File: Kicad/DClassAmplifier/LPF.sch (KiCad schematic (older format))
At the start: 12 parts

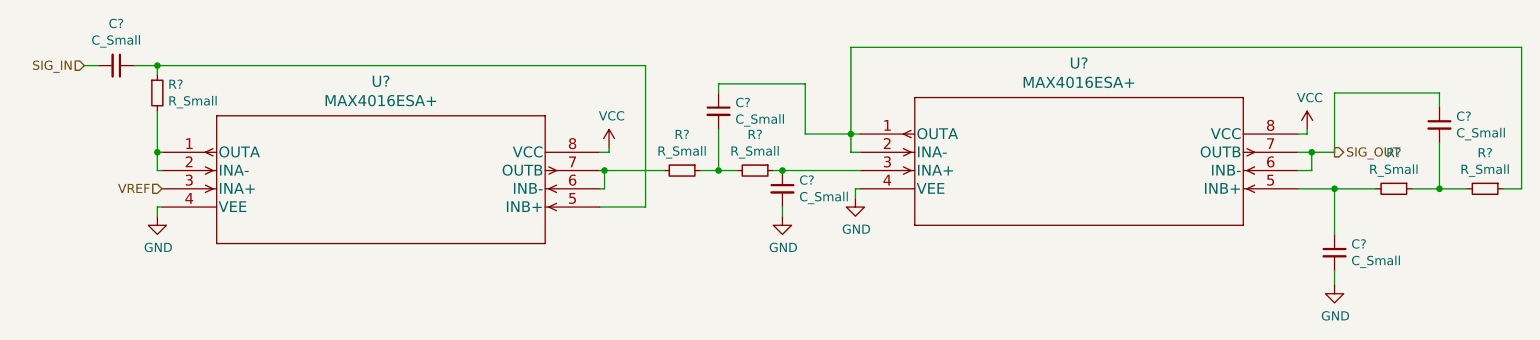
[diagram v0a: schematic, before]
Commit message: Finish off Main Part of Schematic
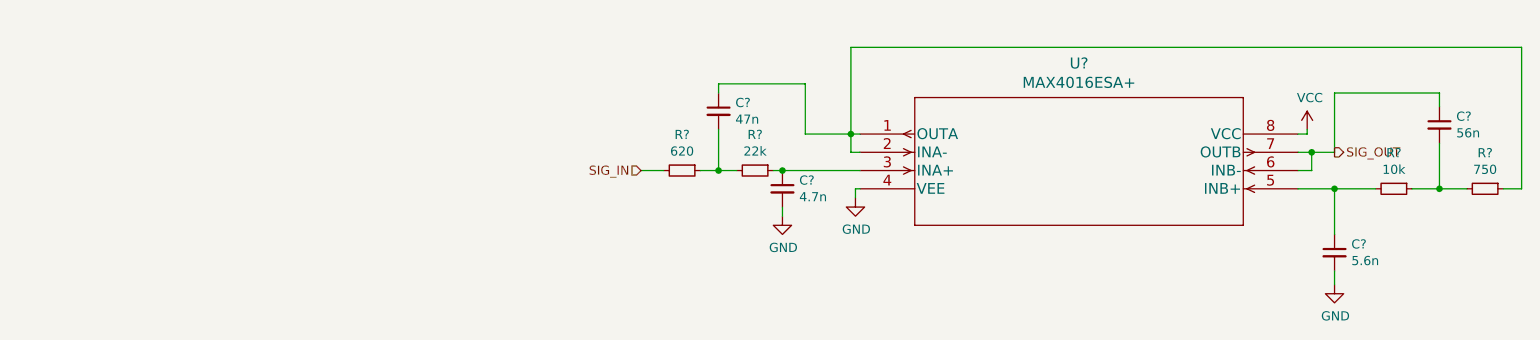
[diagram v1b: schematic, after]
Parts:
- removed C?: C_Small, symbol Device:C_Small
- removed R?: R_Small, symbol Device:R_Small
- removed U?: MAX4016ESA+, 21-0041B_8_MXM, symbol MAX4016ESA:MAX4016ESA+
- C?: value C_Small -> 4.7n; footprint (none) -> Capacitor_SMD:C_0603_1608Metric_Pad1.08x0.95mm_HandSolder
- C?: value C_Small -> 47n; footprint (none) -> Capacitor_SMD:C_0603_1608Metric_Pad1.08x0.95mm_HandSolder
- C?: value C_Small -> 5.6n; footprint (none) -> Capacitor_SMD:C_0603_1608Metric_Pad1.08x0.95mm_HandSolder
- C?: value C_Small -> 56n; footprint (none) -> Capacitor_SMD:C_0603_1608Metric_Pad1.08x0.95mm_HandSolder
- R?: value R_Small -> 22k; footprint (none) -> Resistor_SMD:R_0603_1608Metric_Pad0.98x0.95mm_HandSolder
- R?: value R_Small -> 620; footprint (none) -> Resistor_SMD:R_0603_1608Metric_Pad0.98x0.95mm_HandSolder
- R?: value R_Small -> 10k; footprint (none) -> Resistor_SMD:R_0603_1608Metric_Pad0.98x0.95mm_HandSolder
- R?: value R_Small -> 750; footprint (none) -> Resistor_SMD:R_0603_1608Metric_Pad0.98x0.95mm_HandSolder
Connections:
- net SIG_IN: now also R?.2
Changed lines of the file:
@@
 $Descr A4 11693 8268
 encoding utf-8
-Sheet 5 6
+Sheet 7 7
 Title ""
 Date ""
@@
 $Comp
 L MAX4016ESA:MAX4016ESA+ U?
-U 1 1 61194A75
-P 3650 3325
-F 0 "U?" H 4850 3712 60  0000 C CNN
-F 1 "MAX4016ESA+" H 4850 3606 60  0000 C CNN
-F 2 "21-0041B_8_MXM" H 4850 3565 60  0001 C CNN
-F 3 "" H 3650 3325 60  0000 C CNN
-	1    3650 3325
-	1    0    0    -1
-$EndComp
-$Comp
-L MAX4016ESA:MAX4016ESA+ U?
 U 1 1 61194DD9
 P 7475 3225
@@
 	1    0    0    -1
 $EndComp
-$Comp
-L power:VCC #PWR?
-U 1 1 61196119
-P 6100 3300
-F 0 "#PWR?" H 6100 3150 50  0001 C CNN
-F 1 "VCC" H 6115 3473 50  0000 C CNN
-F 2 "" H 6100 3300 50  0001 C CNN
-F 3 "" H 6100 3300 50  0001 C CNN
-	1    6100 3300
-	1    0    0    -1
-$EndComp
-Wire Wire Line
-	6100 3300 6100 3325
-Wire Wire Line
-	6100 3325 6050 3325
 $Comp
 L power:VCC #PWR?
@@
 	7450 3525 7475 3525
 $Comp
-L power:GND #PWR?
-U 1 1 61198F46
-P 3625 3675
-F 0 "#PWR?" H 3625 3425 50  0001 C CNN
-F 1 "GND" H 3630 3502 50  0000 C CNN
-F 2 "" H 3625 3675 50  0001 C CNN
-F 3 "" H 3625 3675 50  0001 C CNN
-	1    3625 3675
-	1    0    0    -1
-$EndComp
-Wire Wire Line
-	3650 3625 3625 3625
-Wire Wire Line
-	3625 3625 3625 3675
-Text HLabel 3650 3525 0    50   Input ~ 0
-VREF
-Wire Wire Line
-	3650 3425 3625 3425
-Wire Wire Line
-	3625 3425 3625 3325
-Wire Wire Line
-	3625 3325 3650 3325
-$Comp
-L Device:R_Small R?
-U 1 1 6119A6EB
-P 3625 3000
-F 0 "R?" H 3684 3046 50  0000 L CNN
-F 1 "R_Small" H 3684 2955 50  0000 L CNN
-F 2 "" H 3625 3000 50  0001 C CNN
-F 3 "~" H 3625 3000 50  0001 C CNN
-	1    3625 3000
-	1    0    0    -1
-$EndComp
-Wire Wire Line
-	3625 3100 3625 3325
-Connection ~ 3625 3325
-$Comp
-L Device:C_Small C?
-U 1 1 6119BD91
-P 3400 2850
-F 0 "C?" V 3171 2850 50  0000 C CNN
-F 1 "C_Small" V 3262 2850 50  0000 C CNN
-F 2 "" H 3400 2850 50  0001 C CNN
-F 3 "~" H 3400 2850 50  0001 C CNN
-	1    3400 2850
-	0    1    1    0
-$EndComp
-Wire Wire Line
-	3500 2850 3625 2850
-Wire Wire Line
-	3625 2850 3625 2900
-Text HLabel 3225 2850 0    50   Input ~ 0
-SIG_IN
-Wire Wire Line
-	3225 2850 3300 2850
-Wire Wire Line
-	6050 3425 6075 3425
-Wire Wire Line
-	6075 3425 6075 3525
-Wire Wire Line
-	6075 3525 6050 3525
-Wire Wire Line
-	3625 2850 6300 2850
-Wire Wire Line
-	6300 2850 6300 3625
-Wire Wire Line
-	6300 3625 6050 3625
-Connection ~ 3625 2850
-$Comp
 L Device:R_Small R?
 U 1 1 6119FD9F
 P 6900 3425
 F 0 "R?" V 6704 3425 50  0000 C CNN
-F 1 "R_Small" V 6795 3425 50  0000 C CNN
-F 2 "" H 6900 3425 50  0001 C CNN
+F 1 "22k" V 6795 3425 50  0000 C CNN
+F 2 "Resistor_SMD:R_0603_1608Metric_Pad0.98x0.95mm_HandSolder" H 6900 3425 50  0001 C CNN
 F 3 "~" H 6900 3425 50  0001 C CNN
 	1    6900 3425
@@
 P 6500 3425
 F 0 "R?" V 6304 3425 50  0000 C CNN
-F 1 "R_Small" V 6395 3425 50  0000 C CNN
-F 2 "" H 6500 3425 50  0001 C CNN
+F 1 "620" V 6395 3425 50  0000 C CNN
+F 2 "Resistor_SMD:R_0603_1608Metric_Pad0.98x0.95mm_HandSolder" H 6500 3425 50  0001 C CNN
 F 3 "~" H 6500 3425 50  0001 C CNN
 	1    6500 3425
@@
 P 7050 3525
 F 0 "C?" H 7142 3571 50  0000 L CNN
-F 1 "C_Small" H 7142 3480 50  0000 L CNN
-F 2 "" H 7050 3525 50  0001 C CNN
+F 1 "4.7n" H 7142 3480 50  0000 L CNN
+F 2 "Capacitor_SMD:C_0603_1608Metric_Pad1.08x0.95mm_HandSolder" H 7050 3525 50  0001 C CNN
 F 3 "~" H 7050 3525 50  0001 C CNN
 	1    7050 3525
@@
 P 6700 3100
 F 0 "C?" H 6792 3146 50  0000 L CNN
-F 1 "C_Small" H 6792 3055 50  0000 L CNN
-F 2 "" H 6700 3100 50  0001 C CNN
+F 1 "47n" H 6792 3055 50  0000 L CNN
+F 2 "Capacitor_SMD:C_0603_1608Metric_Pad1.08x0.95mm_HandSolder" H 6700 3100 50  0001 C CNN
 F 3 "~" H 6700 3100 50  0001 C CNN
 	1    6700 3100
@@
 Wire Wire Line
 	7425 3225 7175 3225
-Wire Wire Line
-	6400 3425 6075 3425
-Connection ~ 6075 3425
 $Comp
 L Device:C_Small C?
@@
 P 10075 3875
 F 0 "C?" H 10167 3921 50  0000 L CNN
-F 1 "C_Small" H 10167 3830 50  0000 L CNN
-F 2 "" H 10075 3875 50  0001 C CNN
+F 1 "5.6n" H 10167 3830 50  0000 L CNN
+F 2 "Capacitor_SMD:C_0603_1608Metric_Pad1.08x0.95mm_HandSolder" H 10075 3875 50  0001 C CNN
 F 3 "~" H 10075 3875 50  0001 C CNN
 	1    10075 3875
@@
 P 10400 3525
 F 0 "R?" V 10204 3525 50  0000 C CNN
-F 1 "R_Small" V 10295 3525 50  0000 C CNN
-F 2 "" H 10400 3525 50  0001 C CNN
+F 1 "10k" V 10295 3525 50  0000 C CNN
+F 2 "Resistor_SMD:R_0603_1608Metric_Pad0.98x0.95mm_HandSolder" H 10400 3525 50  0001 C CNN
 F 3 "~" H 10400 3525 50  0001 C CNN
 	1    10400 3525
@@
 P 10900 3525
 F 0 "R?" V 10704 3525 50  0000 C CNN
-F 1 "R_Small" V 10795 3525 50  0000 C CNN
-F 2 "" H 10900 3525 50  0001 C CNN
+F 1 "750" V 10795 3525 50  0000 C CNN
+F 2 "Resistor_SMD:R_0603_1608Metric_Pad0.98x0.95mm_HandSolder" H 10900 3525 50  0001 C CNN
 F 3 "~" H 10900 3525 50  0001 C CNN
 	1    10900 3525
@@
 P 10650 3175
 F 0 "C?" H 10742 3221 50  0000 L CNN
-F 1 "C_Small" H 10742 3130 50  0000 L CNN
-F 2 "" H 10650 3175 50  0001 C CNN
+F 1 "56n" H 10742 3130 50  0000 L CNN
+F 2 "Capacitor_SMD:C_0603_1608Metric_Pad1.08x0.95mm_HandSolder" H 10650 3175 50  0001 C CNN
 F 3 "~" H 10650 3175 50  0001 C CNN
 	1    10650 3175
@@
 Text HLabel 10075 3325 2    50   Output ~ 0
 SIG_OUT
+Text HLabel 6275 3425 0    50   Input ~ 0
+SIG_IN
+Wire Wire Line
+	6275 3425 6400 3425
 $EndSCHEMATC

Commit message: updates to schematic
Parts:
- gave numbers to parts that had none: 9
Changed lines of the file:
@@
 $EndDescr
 $Comp
-L MAX4016ESA:MAX4016ESA+ U?
+L MAX4016ESA:MAX4016ESA+ U4
 U 1 1 61194DD9
 P 7475 3225
-F 0 "U?" H 8675 3612 60  0000 C CNN
+F 0 "U4" H 8675 3612 60  0000 C CNN
 F 1 "MAX4016ESA+" H 8675 3506 60  0000 C CNN
 F 2 "21-0041B_8_MXM" H 8675 3465 60  0001 C CNN
@@
 $EndComp
 $Comp
-L power:VCC #PWR?
+L power:VCC #PWR0141
 U 1 1 61197634
 P 9925 3200
-F 0 "#PWR?" H 9925 3050 50  0001 C CNN
+F 0 "#PWR0141" H 9925 3050 50  0001 C CNN
 F 1 "VCC" H 9940 3373 50  0000 C CNN
 F 2 "" H 9925 3200 50  0001 C CNN
@@
 	9925 3225 9875 3225
 $Comp
-L power:GND #PWR?
+L power:GND #PWR0142
 U 1 1 61197F03
 P 7450 3575
-F 0 "#PWR?" H 7450 3325 50  0001 C CNN
+F 0 "#PWR0142" H 7450 3325 50  0001 C CNN
 F 1 "GND" H 7455 3402 50  0000 C CNN
 F 2 "" H 7450 3575 50  0001 C CNN
@@
 	7450 3525 7475 3525
 $Comp
-L Device:R_Small R?
+L Device:R_Small R17
 U 1 1 6119FD9F
 P 6900 3425
-F 0 "R?" V 6704 3425 50  0000 C CNN
+F 0 "R17" V 6704 3425 50  0000 C CNN
 F 1 "22k" V 6795 3425 50  0000 C CNN
 F 2 "Resistor_SMD:R_0603_1608Metric_Pad0.98x0.95mm_HandSolder" H 6900 3425 50  0001 C CNN
@@
 $EndComp
 $Comp
-L Device:R_Small R?
+L Device:R_Small R16
 U 1 1 611A0CB6
 P 6500 3425
-F 0 "R?" V 6304 3425 50  0000 C CNN
+F 0 "R16" V 6304 3425 50  0000 C CNN
 F 1 "620" V 6395 3425 50  0000 C CNN
 F 2 "Resistor_SMD:R_0603_1608Metric_Pad0.98x0.95mm_HandSolder" H 6500 3425 50  0001 C CNN
@@
 $EndComp
 $Comp
-L Device:C_Small C?
+L Device:C_Small C12
 U 1 1 611A751B
 P 7050 3525
-F 0 "C?" H 7142 3571 50  0000 L CNN
+F 0 "C12" H 7142 3571 50  0000 L CNN
 F 1 "4.7n" H 7142 3480 50  0000 L CNN
 F 2 "Capacitor_SMD:C_0603_1608Metric_Pad1.08x0.95mm_HandSolder" H 7050 3525 50  0001 C CNN
@@
 $EndComp
 $Comp
-L Device:C_Small C?
+L Device:C_Small C11
 U 1 1 611A7CBC
 P 6700 3100
-F 0 "C?" H 6792 3146 50  0000 L CNN
+F 0 "C11" H 6792 3146 50  0000 L CNN
 F 1 "47n" H 6792 3055 50  0000 L CNN
 F 2 "Capacitor_SMD:C_0603_1608Metric_Pad1.08x0.95mm_HandSolder" H 6700 3100 50  0001 C CNN
@@
 	7050 3625 7050 3675
 $Comp
-L power:GND #PWR?
+L power:GND #PWR0143
 U 1 1 611AAC29
 P 7050 3675
-F 0 "#PWR?" H 7050 3425 50  0001 C CNN
+F 0 "#PWR0143" H 7050 3425 50  0001 C CNN
 F 1 "GND" H 7055 3502 50  0000 C CNN
 F 2 "" H 7050 3675 50  0001 C CNN
@@
 	7425 3225 7175 3225
 $Comp
-L Device:C_Small C?
+L Device:C_Small C13
 U 1 1 611BBE57
 P 10075 3875
-F 0 "C?" H 10167 3921 50  0000 L CNN
+F 0 "C13" H 10167 3921 50  0000 L CNN
 F 1 "5.6n" H 10167 3830 50  0000 L CNN
 F 2 "Capacitor_SMD:C_0603_1608Metric_Pad1.08x0.95mm_HandSolder" H 10075 3875 50  0001 C CNN
@@
 $EndComp
 $Comp
-L Device:R_Small R?
+L Device:R_Small R18
 U 1 1 611BC850
 P 10400 3525
-F 0 "R?" V 10204 3525 50  0000 C CNN
+F 0 "R18" V 10204 3525 50  0000 C CNN
 F 1 "10k" V 10295 3525 50  0000 C CNN
 F 2 "Resistor_SMD:R_0603_1608Metric_Pad0.98x0.95mm_HandSolder" H 10400 3525 50  0001 C CNN
@@
 $EndComp
 $Comp
-L Device:R_Small R?
+L Device:R_Small R19
 U 1 1 611BD0E0
 P 10900 3525
-F 0 "R?" V 10704 3525 50  0000 C CNN
+F 0 "R19" V 10704 3525 50  0000 C CNN
 F 1 "750" V 10795 3525 50  0000 C CNN
 F 2 "Resistor_SMD:R_0603_1608Metric_Pad0.98x0.95mm_HandSolder" H 10900 3525 50  0001 C CNN
@@
 	11100 3525 11000 3525
 $Comp
-L Device:C_Small C?
+L Device:C_Small C14
 U 1 1 611C0153
 P 10650 3175
-F 0 "C?" H 10742 3221 50  0000 L CNN
+F 0 "C14" H 10742 3221 50  0000 L CNN
 F 1 "56n" H 10742 3130 50  0000 L CNN
 F 2 "Capacitor_SMD:C_0603_1608Metric_Pad1.08x0.95mm_HandSolder" H 10650 3175 50  0001 C CNN
@@
 	10650 3525 10800 3525
 $Comp
-L power:GND #PWR?
+L power:GND #PWR0144
 U 1 1 611C31DE
 P 10075 4050
-F 0 "#PWR?" H 10075 3800 50  0001 C CNN
+F 0 "#PWR0144" H 10075 3800 50  0001 C CNN
 F 1 "GND" H 10080 3877 50  0000 C CNN
 F 2 "" H 10075 4050 50  0001 C CNN

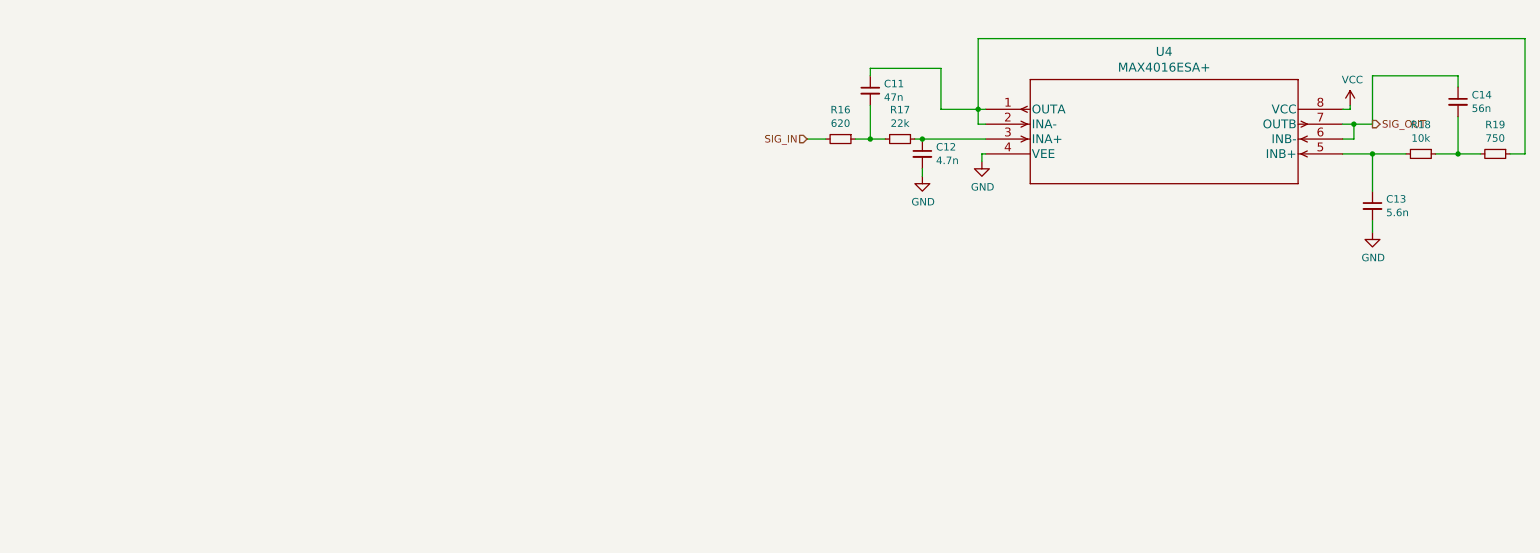
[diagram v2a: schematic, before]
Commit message: Update Opamp for Input Filter
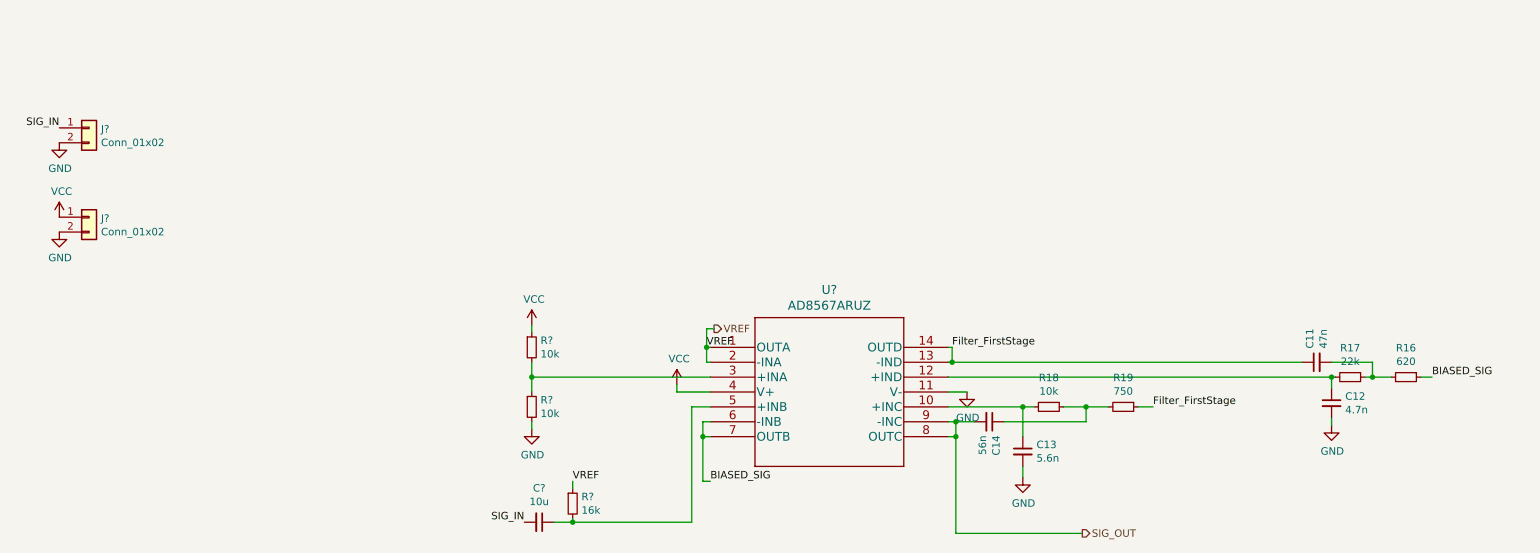
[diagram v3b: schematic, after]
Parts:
- removed U4: MAX4016ESA+, 21-0041B_8_MXM, symbol MAX4016ESA:MAX4016ESA+
- added C?: 10u, Capacitor_SMD:C_0805_2012Metric_Pad1.18x1.45mm_HandSolder, symbol Device:C_Small
- added J? (x2): Conn_01x02, symbol Connector_Generic:Conn_01x02
- added R?: 16k, Resistor_SMD:R_0603_1608Metric_Pad0.98x0.95mm_HandSolder, symbol Device:R_Small
- added R? (x2): 10k, Resistor_SMD:R_0603_1608Metric_Pad0.98x0.95mm_HandSolder, symbol Device:R_Small
- added U?: AD8567ARUZ, RU_14_ADI, symbol AD8567ARUZ:AD8567ARUZ
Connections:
- net GND: now also J?.2 (Pin_2), J?.2 (Pin_2), R?.2, U?.11 (V-)
- net SIG_IN: now also C?.2, J?.1 (Pin_1); no longer R16.2
- net SIG_OUT: now also C14.2, U?.8 (OUTC), U?.9 (-INC); no longer C14.1
- net VCC: now also J?.1 (Pin_1), R?.1, U?.4 (V+)
- net Filter_FirstStage: now reaches C11.1, R19.1
- net Filter_FirstStage: now also U?.13 (-IND), U?.14 (OUTD)
- net at C12.1: now also R17.2, U?.12 (+IND); no longer R17.1
- net at C13.1, R18.2: now also U?.10 (+INC)
- net at R18.1, R19.2: now also C14.1; no longer C14.2
- new net: R?.1, R?.2, U?.3 (+INA)
- new net: C?.1, R?.2, U?.5 (+INB)
- new net: C11.2, R16.2, R17.1
- new net BIASED_SIG: R16.1, U?.6 (-INB), U?.7 (OUTB)
- new net VREF: R?.1, U?.1 (OUTA), U?.2 (-INA)
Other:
- moved on the sheet: C11, C12, C13, C14, R16, R17, R18, R19

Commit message: Added footprints to schematic
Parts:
- J5, J6: renamed from J?; footprint (none) -> Connector_PinSocket_2.54mm:PinSocket_1x02_P2.54mm_Vertical
- gave numbers to parts that had none: 5
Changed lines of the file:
@@
 SIG_OUT
 $Comp
-L AD8567ARUZ:AD8567ARUZ U?
+L AD8567ARUZ:AD8567ARUZ U3
 U 1 1 61100E74
 P 5625 4825
-F 0 "U?" H 6425 5212 60  0000 C CNN
+F 0 "U3" H 6425 5212 60  0000 C CNN
 F 1 "AD8567ARUZ" H 6425 5106 60  0000 C CNN
 F 2 "RU_14_ADI" H 6425 5065 60  0001 C CNN
@@
 $EndComp
 $Comp
-L power:VCC #PWR?
+L power:VCC #PWR0134
 U 1 1 61106B01
 P 5400 5075
-AR Path="/610C616D/61106B01" Ref="#PWR?"  Part="1"
+AR Path="/610C616D/61106B01" Ref="#PWR0134"  Part="1"
 AR Path="/611D4178/61106B01" Ref="#PWR?"  Part="1"
-F 0 "#PWR?" H 5400 4925 50  0001 C CNN
+F 0 "#PWR0134" H 5400 4925 50  0001 C CNN
 F 1 "VCC" H 5415 5248 50  0000 C CNN
 F 2 "" H 5400 5075 50  0001 C CNN
@@
 $EndComp
 $Comp
-L power:GND #PWR?
+L power:GND #PWR0135
 U 1 1 61106B09
 P 7350 5125
-AR Path="/610C616D/61106B09" Ref="#PWR?"  Part="1"
+AR Path="/610C616D/61106B09" Ref="#PWR0135"  Part="1"
 AR Path="/611D4178/61106B09" Ref="#PWR?"  Part="1"
-F 0 "#PWR?" H 7350 4875 50  0001 C CNN
+F 0 "#PWR0135" H 7350 4875 50  0001 C CNN
 F 1 "GND" H 7355 4952 50  0000 C CNN
 F 2 "" H 7350 5125 50  0001 C CNN
@@
 	5600 4825 5625 4825
 $Comp
-L Device:R_Small R?
+L Device:R_Small R15
 U 1 1 61106B14
 P 4700 5875
-AR Path="/610C616D/61106B14" Ref="R?"  Part="1"
+AR Path="/610C616D/61106B14" Ref="R15"  Part="1"
 AR Path="/611D4178/61106B14" Ref="R?"  Part="1"
-F 0 "R?" H 4759 5921 50  0000 L CNN
+F 0 "R15" H 4759 5921 50  0000 L CNN
 F 1 "16k" H 4759 5830 50  0000 L CNN
 F 2 "Resistor_SMD:R_0603_1608Metric_Pad0.98x0.95mm_HandSolder" H 4700 5875 50  0001 C CNN
@@
 Connection ~ 5600 4825
 $Comp
-L Device:C_Small C?
+L Device:C_Small C10
 U 1 1 61106B1C
 P 4475 6000
-AR Path="/610C616D/61106B1C" Ref="C?"  Part="1"
+AR Path="/610C616D/61106B1C" Ref="C10"  Part="1"
 AR Path="/611D4178/61106B1C" Ref="C?"  Part="1"
-F 0 "C?" V 4246 6000 50  0000 C CNN
+F 0 "C10" V 4246 6000 50  0000 C CNN
 F 1 "10u" V 4337 6000 50  0000 C CNN
 F 2 "Capacitor_SMD:C_0805_2012Metric_Pad1.18x1.45mm_HandSolder" H 4475 6000 50  0001 C CNN
@@
 P 4425 4825
 AR Path="/611D4178/61106B32" Ref="R?"  Part="1"
-AR Path="/610C616D/61106B32" Ref="R?"  Part="1"
-F 0 "R?" H 4484 4871 50  0000 L CNN
+AR Path="/610C616D/61106B32" Ref="R13"  Part="1"
+F 0 "R13" H 4484 4871 50  0000 L CNN
 F 1 "10k" H 4484 4780 50  0000 L CNN
 F 2 "Resistor_SMD:R_0603_1608Metric_Pad0.98x0.95mm_HandSolder" H 4425 4825 50  0001 C CNN
@@
 P 4425 5375
 AR Path="/611D4178/61106B3C" Ref="#PWR?"  Part="1"
-AR Path="/610C616D/61106B3C" Ref="#PWR?"  Part="1"
-F 0 "#PWR?" H 4425 5125 50  0001 C CNN
+AR Path="/610C616D/61106B3C" Ref="#PWR0136"  Part="1"
+F 0 "#PWR0136" H 4425 5125 50  0001 C CNN
 F 1 "GND" H 4430 5202 50  0000 C CNN
 F 2 "" H 4425 5375 50  0001 C CNN
@@
 P 4425 4675
 AR Path="/611D4178/61106B43" Ref="#PWR?"  Part="1"
-AR Path="/610C616D/61106B43" Ref="#PWR?"  Part="1"
-F 0 "#PWR?" H 4425 4525 50  0001 C CNN
+AR Path="/610C616D/61106B43" Ref="#PWR0137"  Part="1"
+F 0 "#PWR0137" H 4425 4525 50  0001 C CNN
 F 1 "VCC" H 4440 4848 50  0000 C CNN
 F 2 "" H 4425 4675 50  0001 C CNN
@@
 P 4425 5225
 AR Path="/611D4178/61106B4A" Ref="R?"  Part="1"
-AR Path="/610C616D/61106B4A" Ref="R?"  Part="1"
-F 0 "R?" H 4484 5271 50  0000 L CNN
+AR Path="/610C616D/61106B4A" Ref="R14"  Part="1"
+F 0 "R14" H 4484 5271 50  0000 L CNN
 F 1 "10k" H 4484 5180 50  0000 L CNN
 F 2 "Resistor_SMD:R_0603_1608Metric_Pad0.98x0.95mm_HandSolder" H 4425 5225 50  0001 C CNN
@@
 P 1450 3950
 AR Path="/611D4178/61106B50" Ref="J?"  Part="1"
-AR Path="/610C616D/61106B50" Ref="J?"  Part="1"
-F 0 "J?" H 1530 3942 50  0000 L CNN
+AR Path="/610C616D/61106B50" Ref="J6"  Part="1"
+F 0 "J6" H 1530 3942 50  0000 L CNN
 F 1 "Conn_01x02" H 1530 3851 50  0000 L CNN
-F 2 "" H 1450 3950 50  0001 C CNN
+F 2 "Connector_PinSocket_2.54mm:PinSocket_1x02_P2.54mm_Vertical" H 1450 3950 50  0001 C CNN
 F 3 "~" H 1450 3950 50  0001 C CNN
 	1    1450 3950
@@
 P 1250 4050
 AR Path="/611D4178/61106B56" Ref="#PWR?"  Part="1"
-AR Path="/610C616D/61106B56" Ref="#PWR?"  Part="1"
-F 0 "#PWR?" H 1250 3800 50  0001 C CNN
+AR Path="/610C616D/61106B56" Ref="#PWR0138"  Part="1"
+F 0 "#PWR0138" H 1250 3800 50  0001 C CNN
 F 1 "GND" H 1255 3877 50  0000 C CNN
 F 2 "" H 1250 4050 50  0001 C CNN
@@
 P 1250 3950
 AR Path="/611D4178/61106B5C" Ref="#PWR?"  Part="1"
-AR Path="/610C616D/61106B5C" Ref="#PWR?"  Part="1"
-F 0 "#PWR?" H 1250 3800 50  0001 C CNN
+AR Path="/610C616D/61106B5C" Ref="#PWR0139"  Part="1"
+F 0 "#PWR0139" H 1250 3800 50  0001 C CNN
 F 1 "VCC" H 1265 4123 50  0000 C CNN
 F 2 "" H 1250 3950 50  0001 C CNN
@@
 P 1450 3350
 AR Path="/611D4178/61106B62" Ref="J?"  Part="1"
-AR Path="/610C616D/61106B62" Ref="J?"  Part="1"
-F 0 "J?" H 1530 3342 50  0000 L CNN
+AR Path="/610C616D/61106B62" Ref="J5"  Part="1"
+F 0 "J5" H 1530 3342 50  0000 L CNN
 F 1 "Conn_01x02" H 1530 3251 50  0000 L CNN
-F 2 "" H 1450 3350 50  0001 C CNN
+F 2 "Connector_PinSocket_2.54mm:PinSocket_1x02_P2.54mm_Vertical" H 1450 3350 50  0001 C CNN
 F 3 "~" H 1450 3350 50  0001 C CNN
 	1    1450 3350
@@
 P 1250 3450
 AR Path="/611D4178/61106B68" Ref="#PWR?"  Part="1"
-AR Path="/610C616D/61106B68" Ref="#PWR?"  Part="1"
-F 0 "#PWR?" H 1250 3200 50  0001 C CNN
+AR Path="/610C616D/61106B68" Ref="#PWR0140"  Part="1"
+F 0 "#PWR0140" H 1250 3200 50  0001 C CNN
 F 1 "GND" H 1255 3277 50  0000 C CNN
 F 2 "" H 1250 3450 50  0001 C CNN
